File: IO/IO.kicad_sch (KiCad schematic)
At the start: 36 parts, among them J1 Parallel, J2 Serial, J3 Buss, SW1 Slot, U1 74LS123, U2 74LS85, U3 MC6850, U4 MC6821, U5 74LS393, U6 74LS10, U7 74LS139, Y1 1.8432MHz

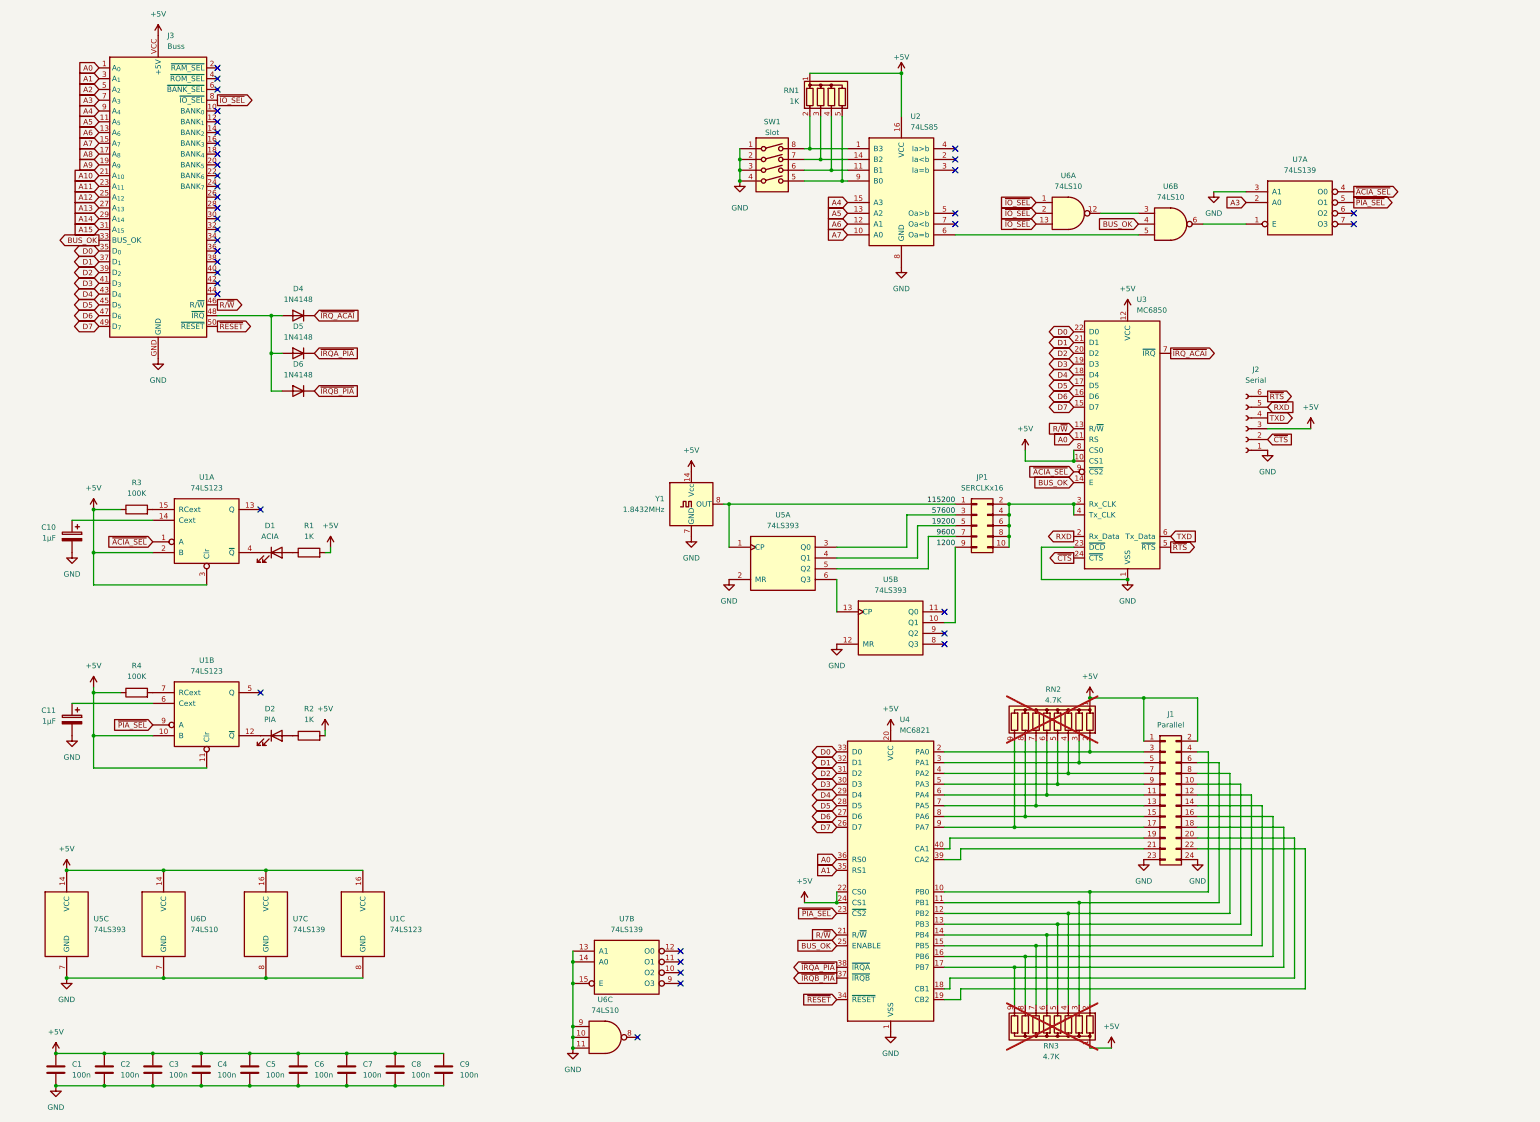
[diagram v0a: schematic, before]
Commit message: finish routing the coms board. add some step models to look at this thing in freecad
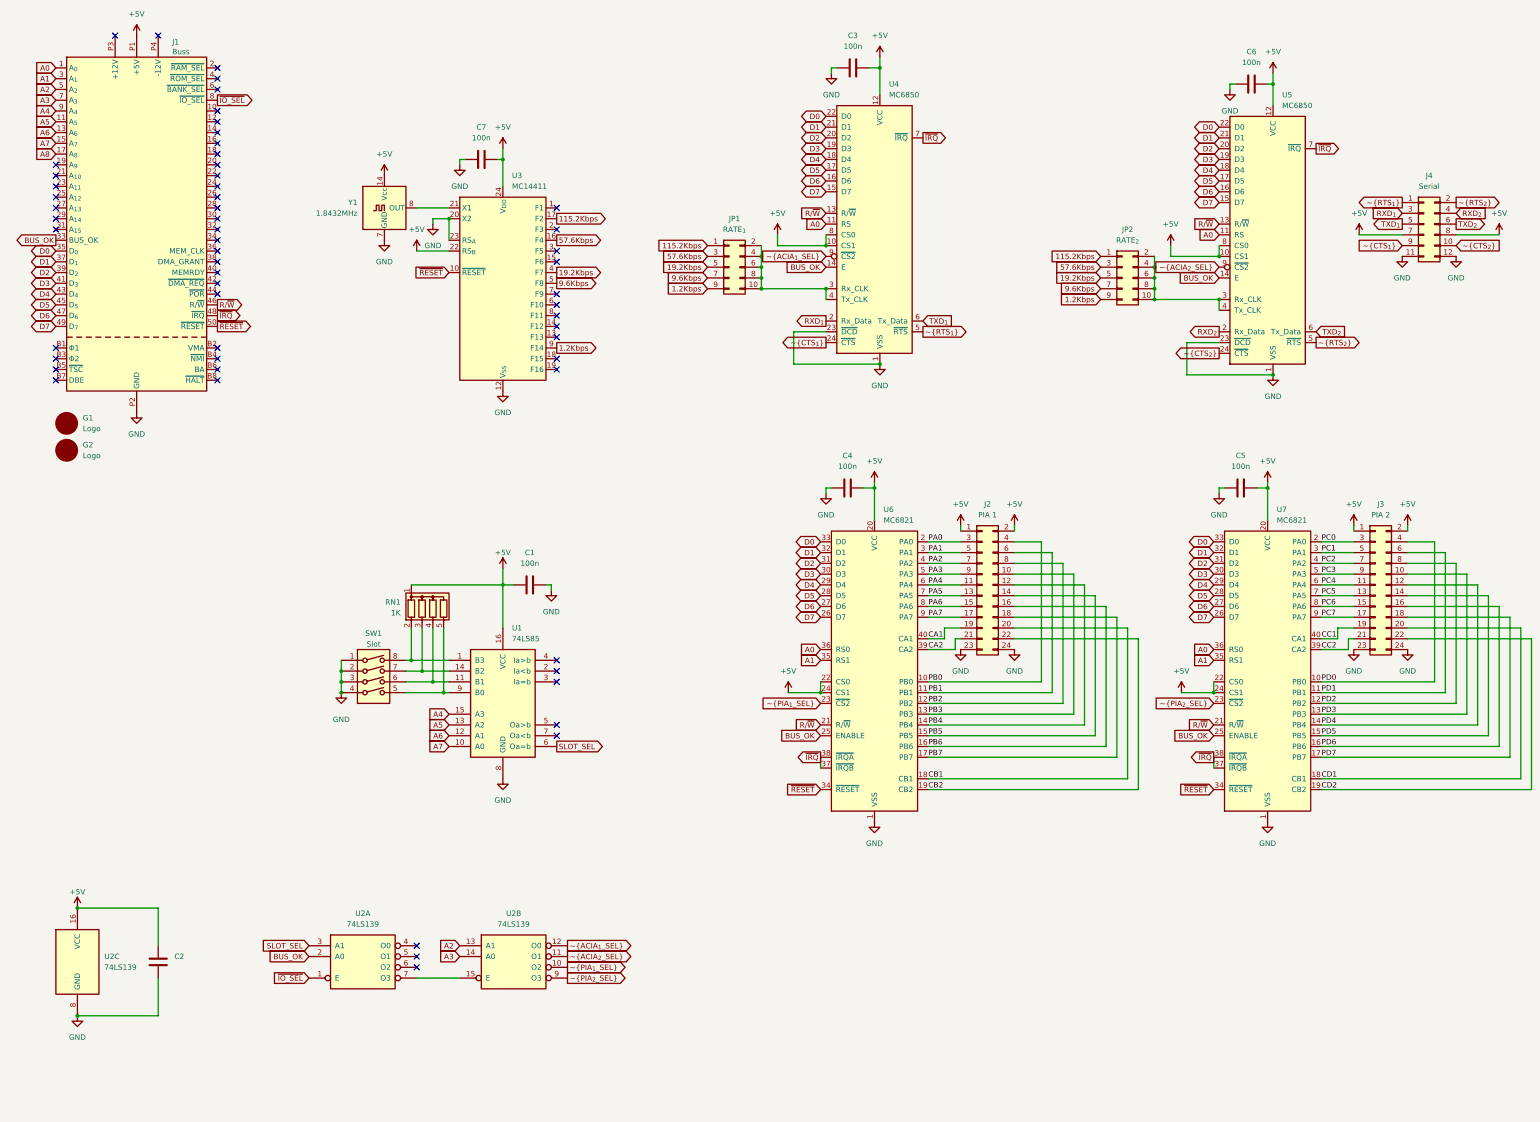
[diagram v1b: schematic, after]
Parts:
- removed C1, C9: 100n, Capacitor_THT:C_Disc_D3.0mm_W1.6mm_P2.50mm, symbol Device:C
- removed C10, C11: 1µF, Capacitor_THT:CP_Radial_D5.0mm_P2.50mm, symbol Device:C_Polarized
- removed D1: ACIA, LED_THT:LED_D3.0mm_Horizontal_O1.27mm_Z2.0mm, symbol Device:LED
- removed D2: PIA, LED_THT:LED_D3.0mm_Horizontal_O1.27mm_Z2.0mm, symbol Device:LED
- removed D4, D5, D6: 1N4148, Diode_THT:D_DO-35_SOD27_P7.62mm_Horizontal, symbol Device:D
- removed J2: Serial, Connector_PinSocket_2.54mm:PinSocket_1x06_P2.54mm_Horizontal, symbol Connector:Conn_01x06_Socket
- removed R1, R2: 1K, Resistor_THT:R_Axial_DIN0207_L6.3mm_D2.5mm_P7.62mm_Horizontal, symbol Device:R
- removed R3, R4: 100K, Resistor_THT:R_Axial_DIN0207_L6.3mm_D2.5mm_P7.62mm_Horizontal, symbol Device:R
- removed RN2, RN3: 4.7K, Resistor_THT:R_Array_SIP9, symbol Device:R_Network08
- removed U1: 74LS123, Package_DIP:DIP-16_W7.62mm, symbol 74xx:74LS123
- removed U5: 74LS393, Package_DIP:DIP-14_W7.62mm, symbol 74xx:74LS393
- removed U6: 74LS10, Package_DIP:DIP-14_W7.62mm, symbol 74xx:74LS10
- added G1: Logo, 0-Footprints:Crank, symbol 0-Symbols:Logo
- added G2: Logo, 0-Footprints:crankery_small, symbol 0-Symbols:Logo
- added J3: PIA 2, Connector_PinHeader_2.54mm:PinHeader_2x12_P2.54mm_Horizontal, symbol Connector_Generic:Conn_02x12_Odd_Even
- added J4: Serial, Connector_PinHeader_2.54mm:PinHeader_2x06_P2.54mm_Horizontal, symbol Connector_Generic:Conn_02x06_Odd_Even
- added JP2: RATE_{2}, 0-Footprints:PinHeader_2x05_P2.54mm_Vertical, symbol Connector_Generic:Conn_02x05_Odd_Even
- added U3: MC14411, 0-Footprints:DIP-24_W15.24mm, symbol 0-Symbols:MC14411
- added U5: MC6850, 0-Footprints:DIP-24_W15.24mm, symbol Interface_UART:MC6850
- added U7: MC6821, 0-Footprints:DIP-40_W15.24mm, symbol Interface:6821
- C1: renamed from C2; footprint Capacitor_THT:C_Disc_D3.0mm_W1.6mm_P2.50mm -> 0-Footprints:C_Disc_D5.0mm_W2.5mm_P5.00mm
- C2: renamed from C7; footprint Capacitor_THT:C_Disc_D3.0mm_W1.6mm_P2.50mm -> 0-Footprints:C_Disc_D5.0mm_W2.5mm_P5.00mm
- C3, C4, C5, C6: footprint Capacitor_THT:C_Disc_D3.0mm_W1.6mm_P2.50mm -> 0-Footprints:C_Disc_D5.0mm_W2.5mm_P5.00mm
- C7: renamed from C8; footprint Capacitor_THT:C_Disc_D3.0mm_W1.6mm_P2.50mm -> 0-Footprints:C_Disc_D5.0mm_W2.5mm_P5.00mm
- J2: renamed from J1; value Parallel -> PIA 1; footprint Connector_PinSocket_2.54mm:PinSocket_2x12_P2.54mm_Horizontal -> Connector_PinHeader_2.54mm:PinHeader_2x12_P2.54mm_Horizontal
- JP1: value SERCLKx16 -> RATE_{1}; footprint Connector_PinHeader_2.54mm:PinHeader_2x05_P2.54mm_Vertical -> 0-Footprints:PinHeader_2x05_P2.54mm_Vertical
- RN1: footprint Resistor_THT:R_Array_SIP5 -> 0-Footprints:R_Array_SIP5
- SW1: footprint Button_Switch_THT:SW_DIP_SPSTx04_Slide_9.78x12.34mm_W7.62mm_P2.54mm -> 0-Footprints:SW_DIP_SPSTx04_Slide_9.78x12.34mm_W7.62mm_P2.54mm
- U1: renamed from U2; footprint Package_DIP:DIP-16_W7.62mm -> 0-Footprints:DIP-16_W7.62mm
- U2: renamed from U7; footprint Package_DIP:DIP-16_W7.62mm -> 0-Footprints:DIP-16_W7.62mm
- U4: renamed from U3; footprint Package_DIP:DIP-24_W15.24mm -> 0-Footprints:DIP-24_W15.24mm
- U6: renamed from U4; footprint Package_DIP:DIP-40_W15.24mm -> 0-Footprints:DIP-40_W15.24mm
- Y1: footprint Oscillator:Oscillator_DIP-14 -> 0-Footprints:Oscillator_DIP-14
- renumbered J3 to J1
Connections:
- net ~{IRQA_PIA} is gone; now on net ~{IRQ}: U6.38 (~{IRQA})
- net ~{IRQB_PIA} is gone; now on net ~{IRQ}: U6.37 (~{IRQB})
- net ~{IRQ_ACAI} is gone; now on net ~{IRQ}: U4.7 (~{IRQ})
- net +5V: now also C3.2, C4.2, C5.2, C6.2, C7.2, J1.P1 (+5V), J3.1 (Pin_1), J3.2 (Pin_2), J4.7 (Pin_7), J4.8 (Pin_8), U3.22 (RS_{B}), U3.24 (V_{DD}), U5.10 (CS1), U5.12 (VCC), U5.8 (CS0), U7.20 (VCC), U7.22 (CS0), U7.24 (CS1); no longer C3.1, C4.1, C5.1, C6.1, C7.1, J1.VCC (+5V)
- net A0: now also U5.11 (RS), U7.36 (RS0)
- net A1: now also U7.35 (RS1)
- net A2: now also U2.13 (A1)
- net A3: now also U2.14 (A0); no longer U2.2 (A0)
- net BUS_OK: now also U2.2 (A0), U5.14 (E), U7.25 (ENABLE)
- net D0: now also U5.22 (D0), U7.33 (D0)
- net D1: now also U5.21 (D1), U7.32 (D1)
- net D2: now also U5.20 (D2), U7.31 (D2)
- net D3: now also U5.19 (D3), U7.30 (D3)
- net D4: now also U5.18 (D4), U7.29 (D4)
- net D5: now also U5.17 (D5), U7.28 (D5)
- net D6: now also U5.16 (D6), U7.27 (D6)
- net D7: now also U5.15 (D7), U7.26 (D7)
- net GND: now also C3.1, C4.1, C5.1, C6.1, C7.1, J1.P2 (GND), J3.23 (Pin_23), J3.24 (Pin_24), J4.11 (Pin_11), J4.12 (Pin_12), U3.12 (V_{SS}), U3.20 (X2), U3.23 (RS_{A}), U5.1 (VSS), U5.23 (~{DCD}), U7.1 (VSS); no longer C3.2, C4.2, C5.2, C6.2, C7.2, J1.GND, U2.13 (A1), U2.14 (A0), U2.15 (E), U2.3 (A1)
- net R/~{W}: now also U5.13 (R/~{W}), U7.21 (R/~{W})
- net ~{IO_SEL}: now also U2.1 (E)
- net ~{RESET}: now also U3.10 (~{RESET}), U7.34 (~{RESET})
- net ~{IRQ}: now reaches J1.48 (~{IRQ})
- net ~{IRQ}: now also U5.7 (~{IRQ}), U7.37 (~{IRQB}), U7.38 (~{IRQA})
- net SLOT_SEL: now reaches U1.6 (Oa=b)
- net SLOT_SEL: now also U2.3 (A1)
- net PB3: now reaches J2.10 (Pin_10), U6.13 (PB3)
- net PA4: now reaches J2.11 (Pin_11), U6.6 (PA4)
- net PB4: now reaches J2.12 (Pin_12), U6.14 (PB4)
- net PA5: now reaches J2.13 (Pin_13), U6.7 (PA5)
- net PB5: now reaches J2.14 (Pin_14), U6.15 (PB5)
- net PA6: now reaches J2.15 (Pin_15), U6.8 (PA6)
- net PB6: now reaches J2.16 (Pin_16), U6.16 (PB6)
- net PA7: now reaches J2.17 (Pin_17), U6.9 (PA7)
- net PB7: now reaches J2.18 (Pin_18), U6.17 (PB7)
- net CA1: now reaches J2.19 (Pin_19), U6.40 (CA1)
- net CB1: now reaches J2.20 (Pin_20), U6.18 (CB1)
- net CA2: now reaches J2.21 (Pin_21), U6.39 (CA2)
- net CB2: now reaches J2.22 (Pin_22), U6.19 (CB2)
- net PA0: now reaches J2.3 (Pin_3), U6.2 (PA0)
- net PB0: now reaches J2.4 (Pin_4), U6.10 (PB0)
- net PA1: now reaches J2.5 (Pin_5), U6.3 (PA1)
- net PB1: now reaches J2.6 (Pin_6), U6.11 (PB1)
- net PA2: now reaches J2.7 (Pin_7), U6.4 (PA2)
- net PB2: now reaches J2.8 (Pin_8), U6.12 (PB2)
- net PA3: now reaches J2.9 (Pin_9), U6.5 (PA3)
- net at U2.7 (O3): now also U2.15 (E)
- net ~{PIA_{1}_SEL}: now reaches U2.10 (O2)
- net ~{PIA_{1}_SEL}: now also U6.23 (~{CS2})
- net ~{ACIA_{2}_SEL}: now reaches U2.11 (O1)
- net ~{ACIA_{2}_SEL}: now also U5.9 (~{CS2})
- net ~{ACIA_{1}_SEL}: now reaches U2.12 (O0)
- net ~{ACIA_{1}_SEL}: now also U4.9 (~{CS2})
- net ~{PIA_{2}_SEL}: now reaches U2.9 (O3)
- net ~{PIA_{2}_SEL}: now also U7.23 (~{CS2})
- net 115200: no longer names the net of Y1.8 (OUT)
- net 115200: now also U3.21 (X1); no longer JP1.1 (Pin_1)
- net 1200 renamed 1.2Kbps
- net 1.2Kbps: now also JP2.9 (Pin_9), U3.9 (F14)
- net 19200 renamed 19.2Kbps
- net 19.2Kbps: now also JP2.5 (Pin_5), U3.4 (F7)
- net 57600 renamed 57.6Kbps
- net 57.6Kbps: now also JP2.3 (Pin_3), U3.16 (F4)
- net 9600 renamed 9.6Kbps
- net 9.6Kbps: now also JP2.7 (Pin_7), U3.5 (F8)
- net A10: no longer names the net of J1.21 (A_{10})
- net A11: no longer names the net of J1.23 (A_{11})
- net A12: no longer names the net of J1.25 (A_{12})
- net A13: no longer names the net of J1.27 (A_{13})
- net A14: no longer names the net of J1.29 (A_{14})
- net A15: no longer names the net of J1.31 (A_{15})
- net A9: no longer names the net of J1.19 (A_{9})
- net RXD renamed RXD_{1}
- net RXD_{1}: now also J4.3 (Pin_3)
- net TXD renamed TXD_{1}
- net TXD_{1}: now also J4.5 (Pin_5)
- net ~{ACIA_SEL}: no longer names the net of U2.4 (O0)
- net ~{ACIA_SEL}: no longer U4.9 (~{CS2})
- net ~{CTS} renamed ~{CTS_{1}}
- net ~{CTS_{1}}: now also J4.9 (Pin_9)
- net ~{PIA_SEL}: no longer names the net of U2.5 (O1)
- net ~{PIA_SEL}: no longer U6.23 (~{CS2})
- net ~{RTS} renamed ~{RTS_{1}}
- net ~{RTS_{1}}: now also J4.1 (Pin_1)
- new net: JP2.10 (Pin_10), JP2.2 (Pin_2), JP2.4 (Pin_4), JP2.6 (Pin_6), JP2.8 (Pin_8), U5.3 (Rx_CLK), U5.4 (Tx_CLK)
- new net 115.2Kbps: JP1.1 (Pin_1), JP2.1 (Pin_1), U3.17 (F2)
- new net CC1: J3.19 (Pin_19), U7.40 (CA1)
- new net CC2: J3.21 (Pin_21), U7.39 (CA2)
- new net CD1: J3.20 (Pin_20), U7.18 (CB1)
- new net CD2: J3.22 (Pin_22), U7.19 (CB2)
- new net PC0: J3.3 (Pin_3), U7.2 (PA0)
- new net PC1: J3.5 (Pin_5), U7.3 (PA1)
- new net PC2: J3.7 (Pin_7), U7.4 (PA2)
- new net PC3: J3.9 (Pin_9), U7.5 (PA3)
- new net PC4: J3.11 (Pin_11), U7.6 (PA4)
- new net PC5: J3.13 (Pin_13), U7.7 (PA5)
- new net PC6: J3.15 (Pin_15), U7.8 (PA6)
- new net PC7: J3.17 (Pin_17), U7.9 (PA7)
- new net PD0: J3.4 (Pin_4), U7.10 (PB0)
- new net PD1: J3.6 (Pin_6), U7.11 (PB1)
- new net PD2: J3.8 (Pin_8), U7.12 (PB2)
- new net PD3: J3.10 (Pin_10), U7.13 (PB3)
- new net PD4: J3.12 (Pin_12), U7.14 (PB4)
- new net PD5: J3.14 (Pin_14), U7.15 (PB5)
- new net PD6: J3.16 (Pin_16), U7.16 (PB6)
- new net PD7: J3.18 (Pin_18), U7.17 (PB7)
- new net RXD_{2}: J4.4 (Pin_4), U5.2 (Rx_Data)
- new net TXD_{2}: J4.6 (Pin_6), U5.6 (Tx_Data)
- new net ~{CTS_{2}}: J4.10 (Pin_10), U5.24 (~{CTS})
- new net ~{RTS_{2}}: J4.2 (Pin_2), U5.5 (~{RTS})
- no-connect marks 38 -> 57
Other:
- moved on the sheet: C1, C2, C3, C4, C7, J2, JP1, RN1, SW1, U1, U2A, U2B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
